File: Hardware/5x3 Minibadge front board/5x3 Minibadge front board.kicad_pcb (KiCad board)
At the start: 2 copper layers, 137.2 x 86.4 mm, 29 parts

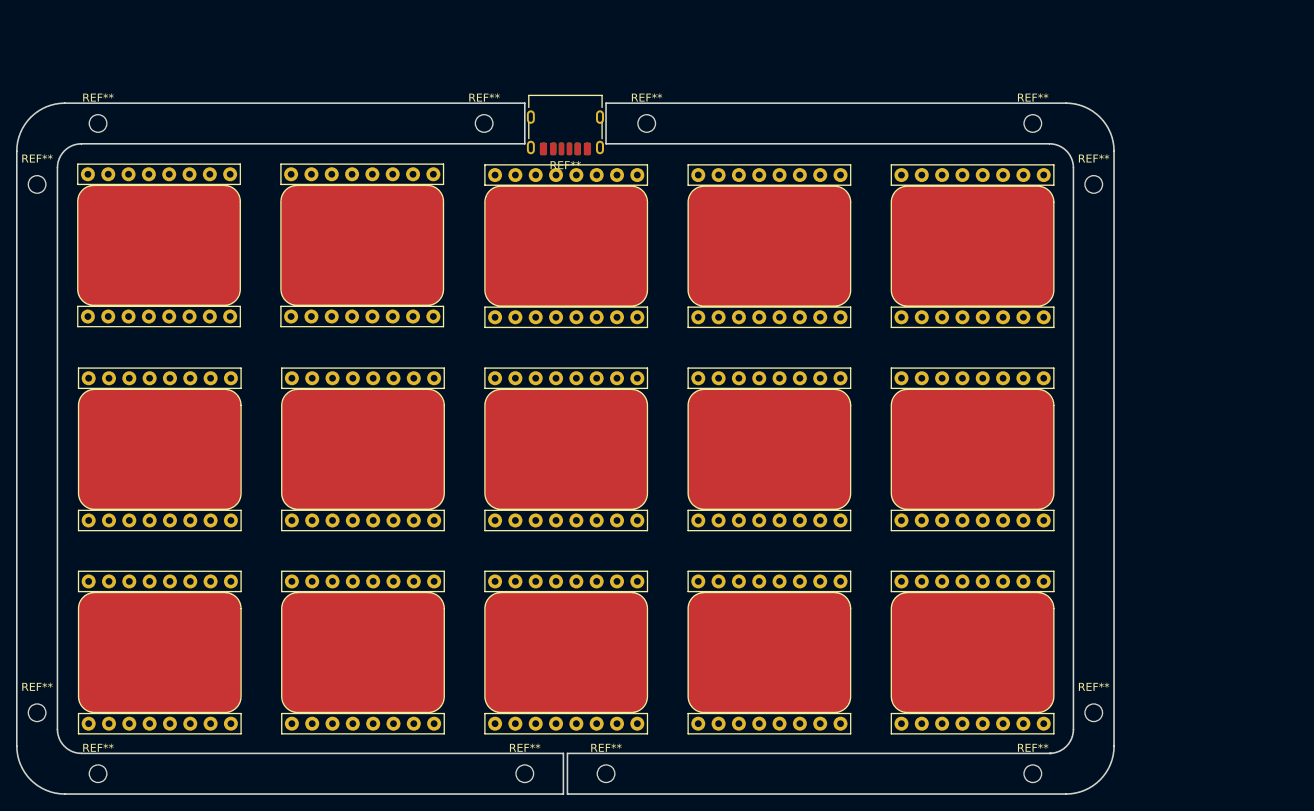
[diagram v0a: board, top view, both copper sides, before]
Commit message: FIxing issues
- Messed up mounting holes
- board didn't copy to front plate
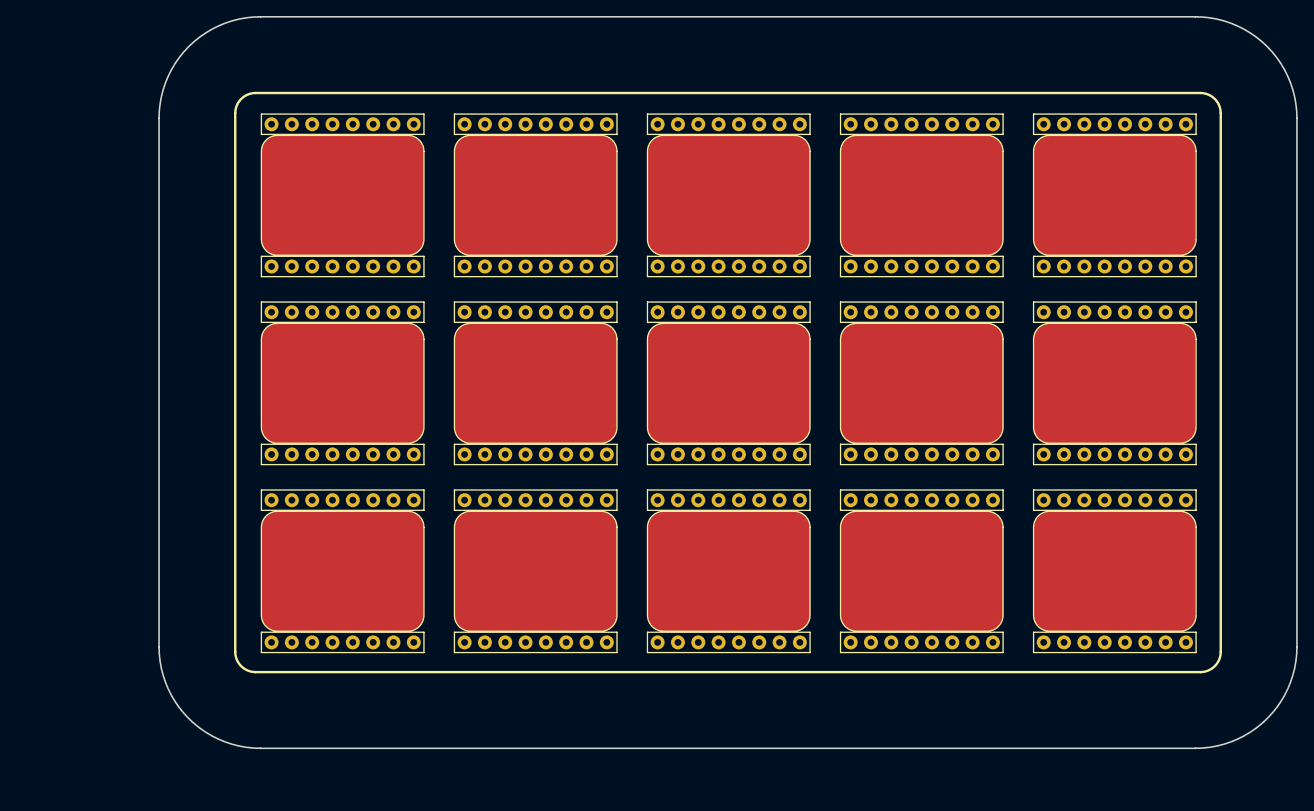
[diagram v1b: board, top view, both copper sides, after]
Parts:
- removed REF** (x12): MountingHole_2.2mm_M2, MountingHole:MountingHole_2.2mm_M2
- removed REF**: USB_C_Receptacle_HRO_TYPE-C-31-M-17, Connector_USB:USB_C_Receptacle_HRO_TYPE-C-31-M-17
- removed REF**, REF**1, REF**10, REF**11, REF**12, REF**13, REF**14, REF**2, REF**3, REF**4, REF**5, REF**6, REF**7, REF**8, REF**9: MiniBadge_Slot_Reflective, MiniBadge:MiniBadge_Slot_Reflective
- removed REF**: PinHeader_2x05_P2.54mm_Vertical_SMD, Connector_PinHeader_2.54mm:PinHeader_2x05_P2.54mm_Vertical_SMD
- added J1: Board to Board, Connector_PinSocket_2.54mm:PinSocket_2x05_P2.54mm_Vertical_SMD, B.Cu at (182.7, 75.6)
- added MB1: MiniBadge_Full, MiniBadge:MiniBadge_Slot_Reflective, F.Cu at (73.8, 42.0)
- added MB10: MiniBadge_Full, MiniBadge:MiniBadge_Slot_Reflective, F.Cu at (170.3, 65.5)
- added MB11: MiniBadge_Full, MiniBadge:MiniBadge_Slot_Reflective, F.Cu at (73.8, 89.0)
- added MB12: MiniBadge_Full, MiniBadge:MiniBadge_Slot_Reflective, F.Cu at (97.9, 89.0)
- added MB13: MiniBadge_Full, MiniBadge:MiniBadge_Slot_Reflective, F.Cu at (122.0, 89.0)
- added MB14: MiniBadge_Full, MiniBadge:MiniBadge_Slot_Reflective, F.Cu at (146.1, 89.0)
- added MB15: MiniBadge_Full, MiniBadge:MiniBadge_Slot_Reflective, F.Cu at (170.3, 89.0)
- added MB2: MiniBadge_Full, MiniBadge:MiniBadge_Slot_Reflective, F.Cu at (97.9, 42.0)
- added MB3: MiniBadge_Full, MiniBadge:MiniBadge_Slot_Reflective, F.Cu at (122.0, 42.0)
- added MB4: MiniBadge_Full, MiniBadge:MiniBadge_Slot_Reflective, F.Cu at (146.1, 42.0)
- added MB5: MiniBadge_Full, MiniBadge:MiniBadge_Slot_Reflective, F.Cu at (170.3, 42.0)
- added MB6: MiniBadge_Full, MiniBadge:MiniBadge_Slot_Reflective, F.Cu at (73.8, 65.5)
- added MB7: MiniBadge_Full, MiniBadge:MiniBadge_Slot_Reflective, F.Cu at (97.9, 65.5)
- added MB8: MiniBadge_Full, MiniBadge:MiniBadge_Slot_Reflective, F.Cu at (122.0, 65.5)
- added MB9: MiniBadge_Full, MiniBadge:MiniBadge_Slot_Reflective, F.Cu at (146.1, 65.5)
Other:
- board size 137.2 x 86.4 mm -> 142.2 x 91.4 mm

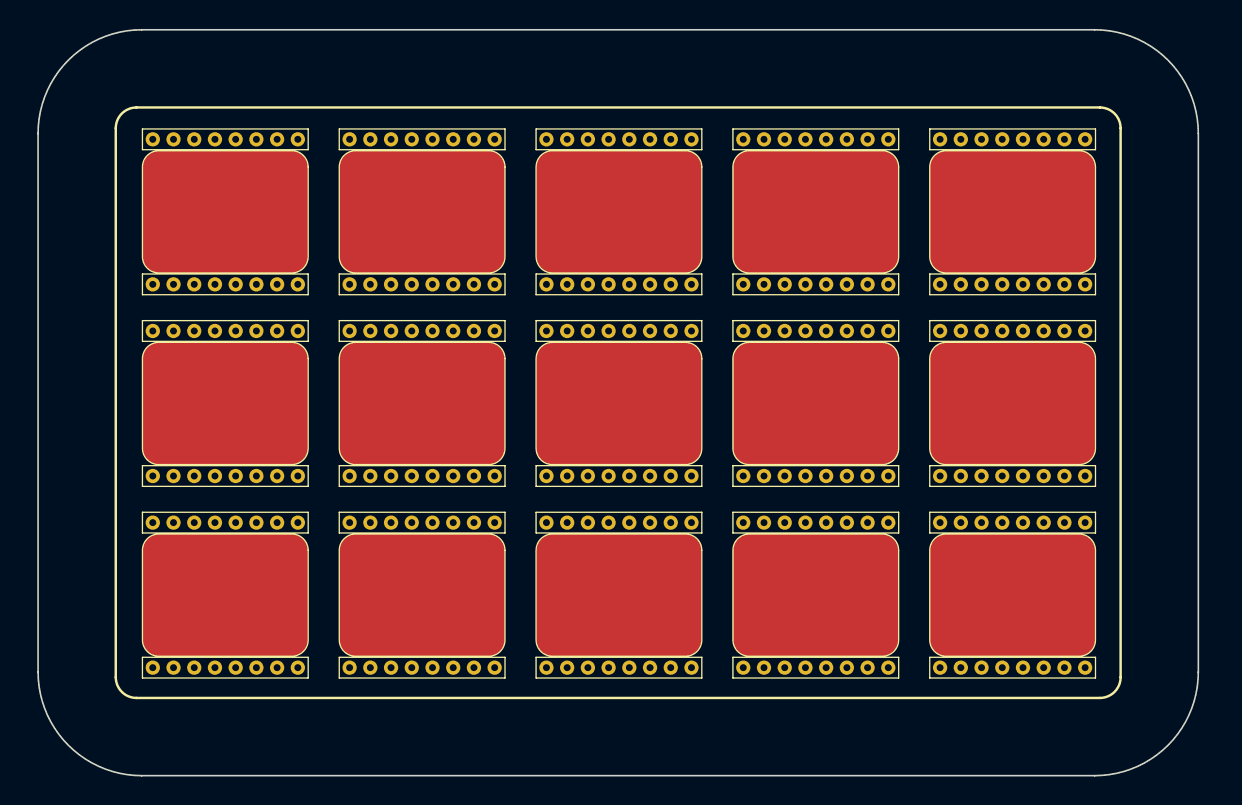
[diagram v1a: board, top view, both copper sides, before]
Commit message: Routed Minibadge Display
god that sucked, and my routing sucks too.
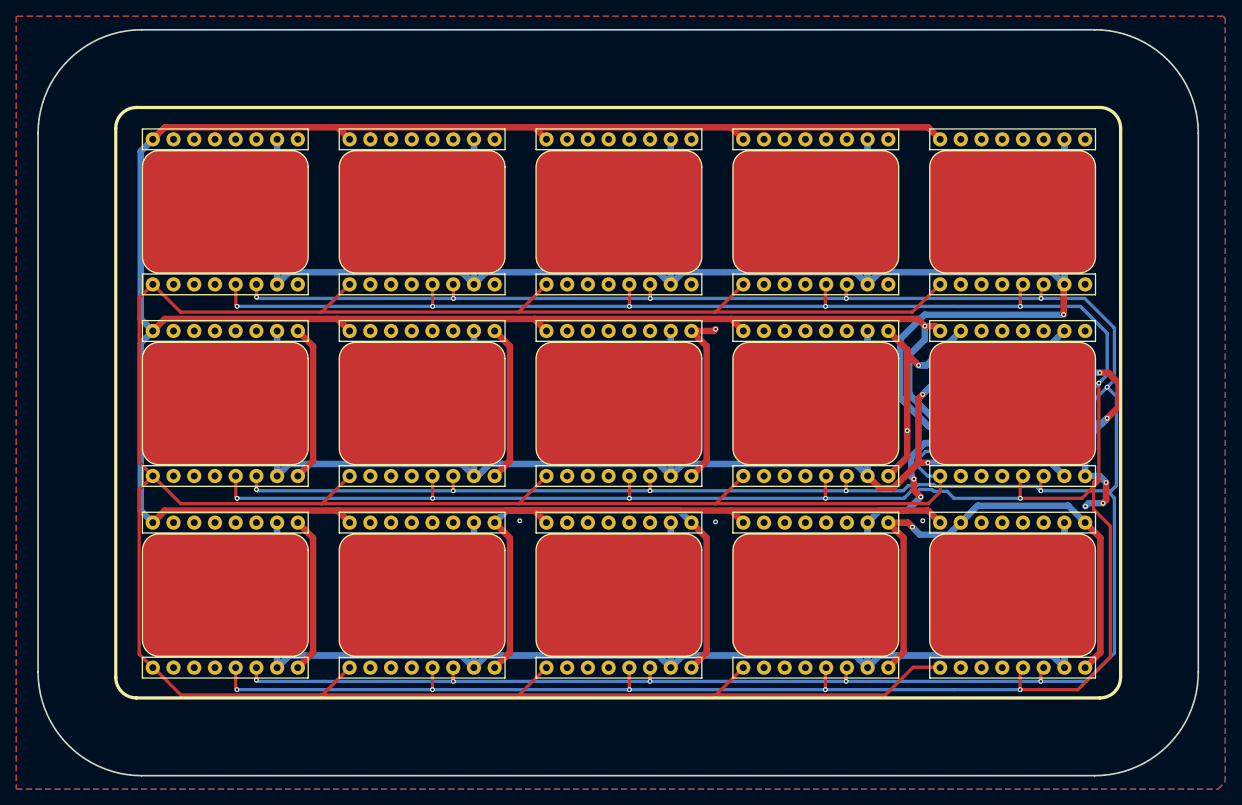
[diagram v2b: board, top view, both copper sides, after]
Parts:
- J1: footprint Connector_PinSocket_2.54mm:PinSocket_2x05_P2.54mm_Vertical_SMD -> Connector_PinHeader_2.54mm:PinHeader_2x05_P2.54mm_Vertical_SMD
- turned J1 to -90 degrees
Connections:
- J1 pad 1: +3v3-1 -> +3v3-2
- J1 pad 2: +3v3-2 -> +3v3-1
- J1 pad 3: +3v3-3 -> +VBATT
- J1 pad 4: +VBATT -> +3v3-3
- J1 pad 5: +5V -> MB_CLK
- J1 pad 6: MB_CLK -> +5V
- J1 pad 7: MB_SDA -> MB_SCL
- J1 pad 8: MB_SCL -> MB_SDA
- MB10 pad 15: +3v3-1 -> +3v3-2
- MB10 pad 7: +3v3-1 -> +3v3-2
- MB11 pad 15: +3v3-2 -> +3v3-3
- MB11 pad 7: +3v3-2 -> +3v3-3
- MB13 pad 15: +3v3-1 -> +3v3-3
- MB13 pad 7: +3v3-1 -> +3v3-3
- MB14 pad 15: +3v3-2 -> +3v3-3
- MB14 pad 7: +3v3-2 -> +3v3-3
- MB2 pad 15: +3v3-2 -> +3v3-1
- MB2 pad 7: +3v3-2 -> +3v3-1
- MB3 pad 15: +3v3-3 -> +3v3-1
- MB3 pad 7: +3v3-3 -> +3v3-1
- MB5 pad 15: +3v3-2 -> +3v3-1
- MB5 pad 7: +3v3-2 -> +3v3-1
- MB6 pad 15: +3v3-3 -> +3v3-2
- MB6 pad 7: +3v3-3 -> +3v3-2
- MB7 pad 15: +3v3-1 -> +3v3-2
- MB7 pad 7: +3v3-1 -> +3v3-2
- MB9 pad 15: +3v3-3 -> +3v3-2
- MB9 pad 7: +3v3-3 -> +3v3-2
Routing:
- net MB_CLK: track 0.00 -> 420.5 mm
- net MB_SCL: track 0.00 -> 416.5 mm, vias 0 -> 16
- net MB_SDA: track 0.00 -> 395.2 mm, vias 0 -> 16
- net +5V: track 0.00 -> 389.3 mm, vias 0 -> 1
- net GND: track 0.00 -> 271.3 mm, vias 0 -> 12
- net +3v3-1: track 0.00 -> 235.1 mm, vias 0 -> 1
- net +3v3-3: track 0.00 -> 217.8 mm, vias 0 -> 2
- net +3v3-2: track 0.00 -> 203.5 mm, vias 0 -> 2
- added copper zone on B.Cu, net GND
- added copper zone on F.Cu, net GND
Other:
- board text added: "+3V3-1 +3V3-3 +5V MB_SDA GND"
- board text added: "+3V3-2 +VBATT MB_CLK MB_SCL GND"

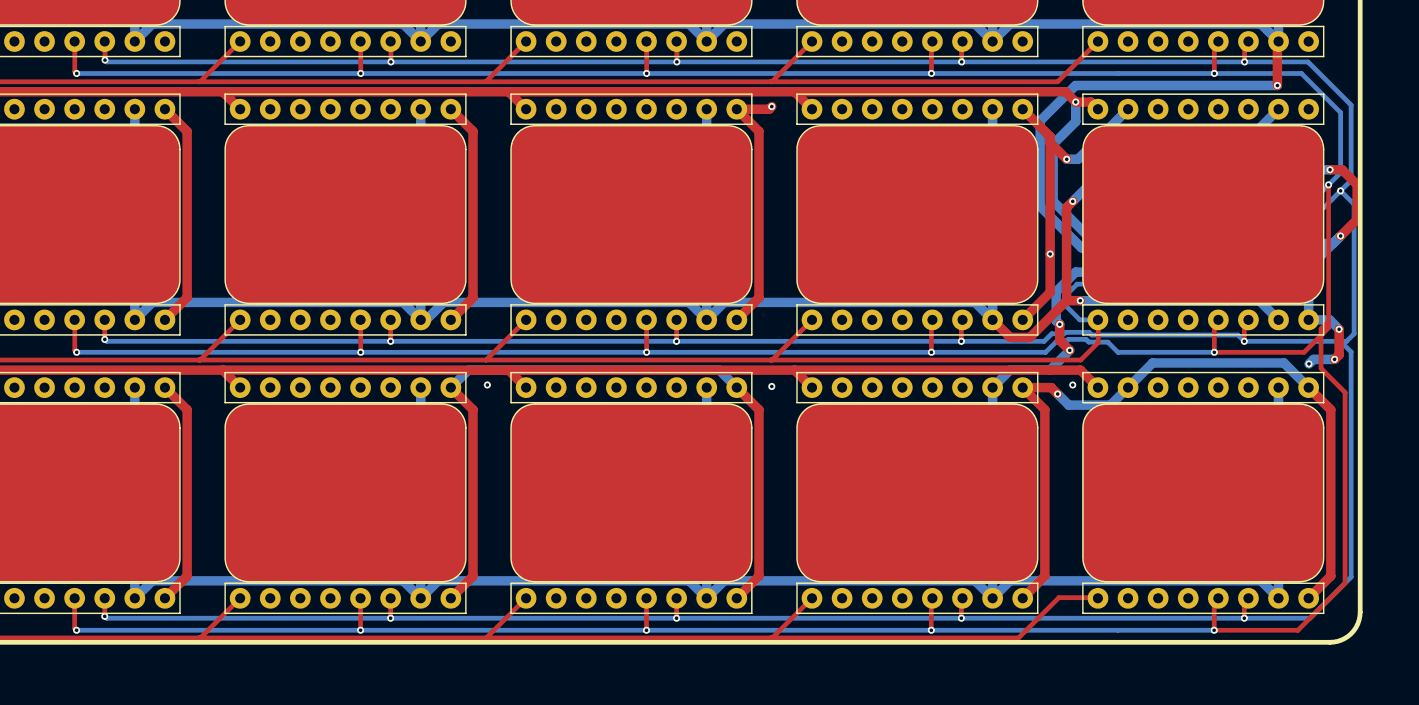
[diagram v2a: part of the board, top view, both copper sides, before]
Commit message: Fix DRC errors
got it down from 20+ Errors and 200+ warnings to zero errors and some unnecessary warnings!
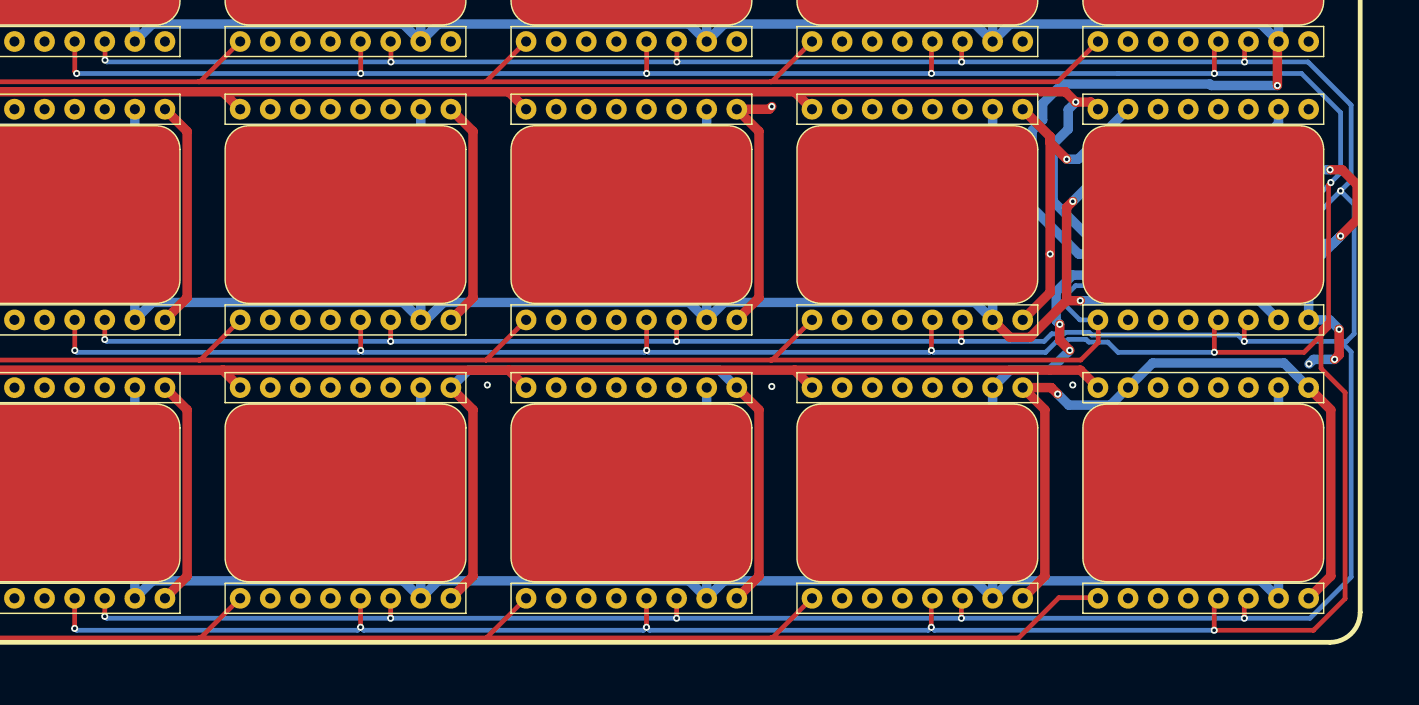
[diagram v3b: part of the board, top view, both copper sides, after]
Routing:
- net +3v3-1: track 235.1 -> 237.4 mm
- net +3v3-2: track 203.5 -> 205.1 mm
- net MB_SCL: track 416.5 -> 417.3 mm
- net +3v3-3: track 217.8 -> 218.4 mm

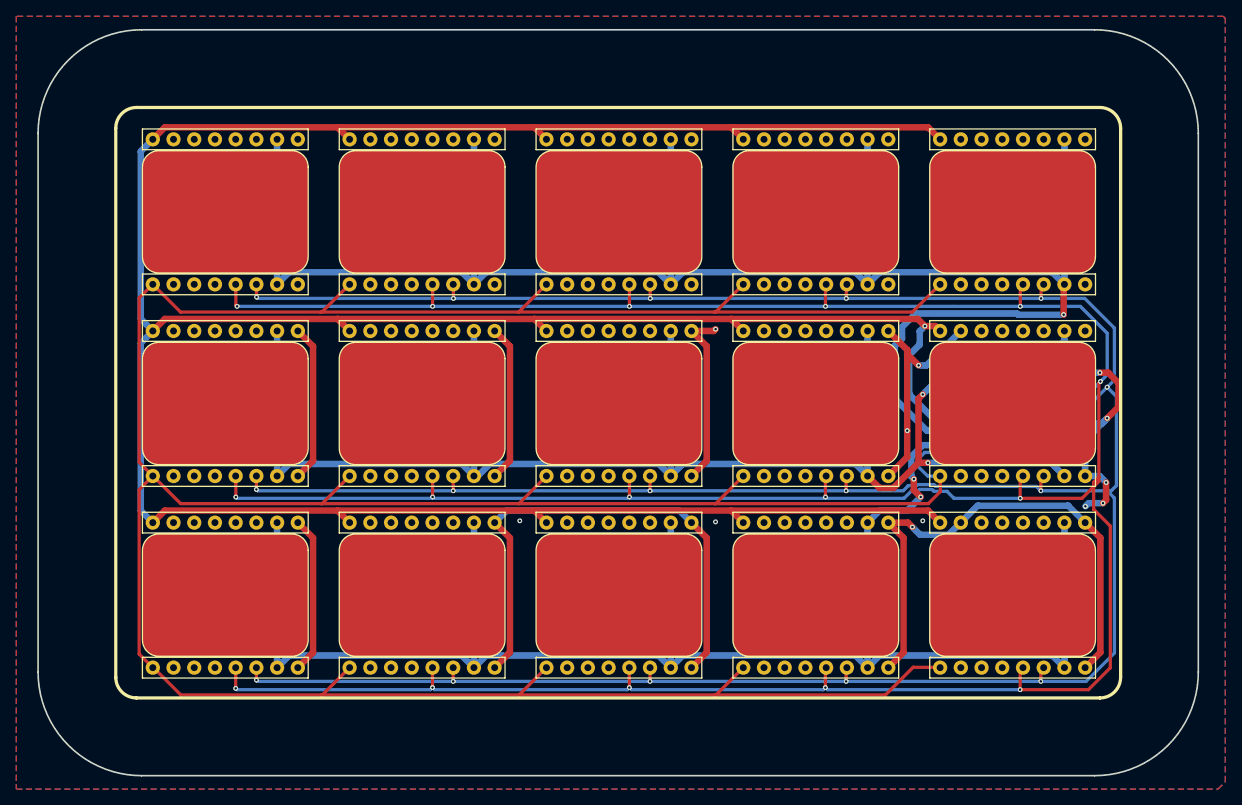
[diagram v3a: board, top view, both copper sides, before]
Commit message: hardware changes and initial traces/layout
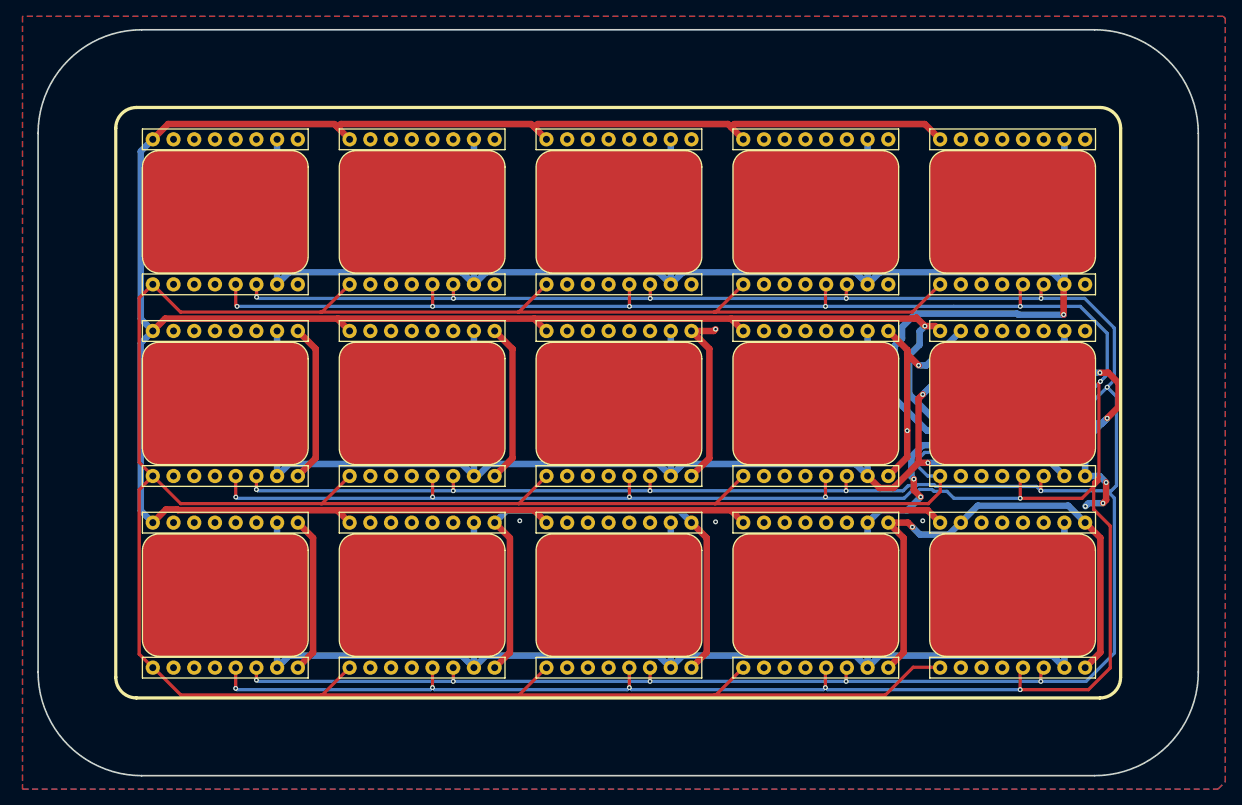
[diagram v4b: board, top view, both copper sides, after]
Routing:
- net +5V: track 389.7 -> 391.5 mm
- net GND: track 271.3 -> 272.1 mm
